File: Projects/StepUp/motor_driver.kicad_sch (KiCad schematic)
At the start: 39 parts, among them J3 1862068, Q1 BSS84, Q2 2N7002-7-F, U4 TMC2300-LA

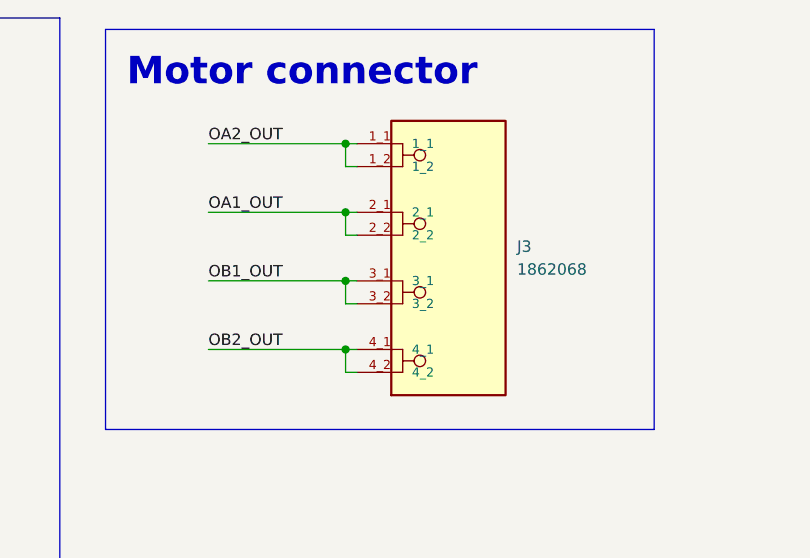
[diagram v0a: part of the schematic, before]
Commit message: feat(cad): CAD dims pushed to PCB
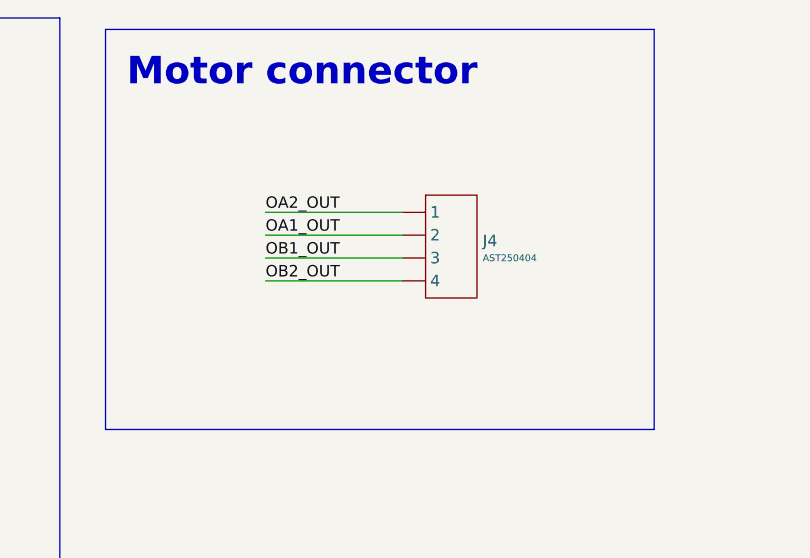
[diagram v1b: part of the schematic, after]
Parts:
- removed J3: 1862068, Snapeda:1862068_PHOENIX_1862068, symbol Snapeda_kicad:1862068
- added J4: AST250404, my_parts:AST250404, symbol my_parts:AST250404
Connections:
- net OA1_OUT: now also J4. (4)
- net OA2_OUT: now also J4. (4)
- net OB1_OUT: now also J4. (4)
- net OB2_OUT: now also J4. (4)

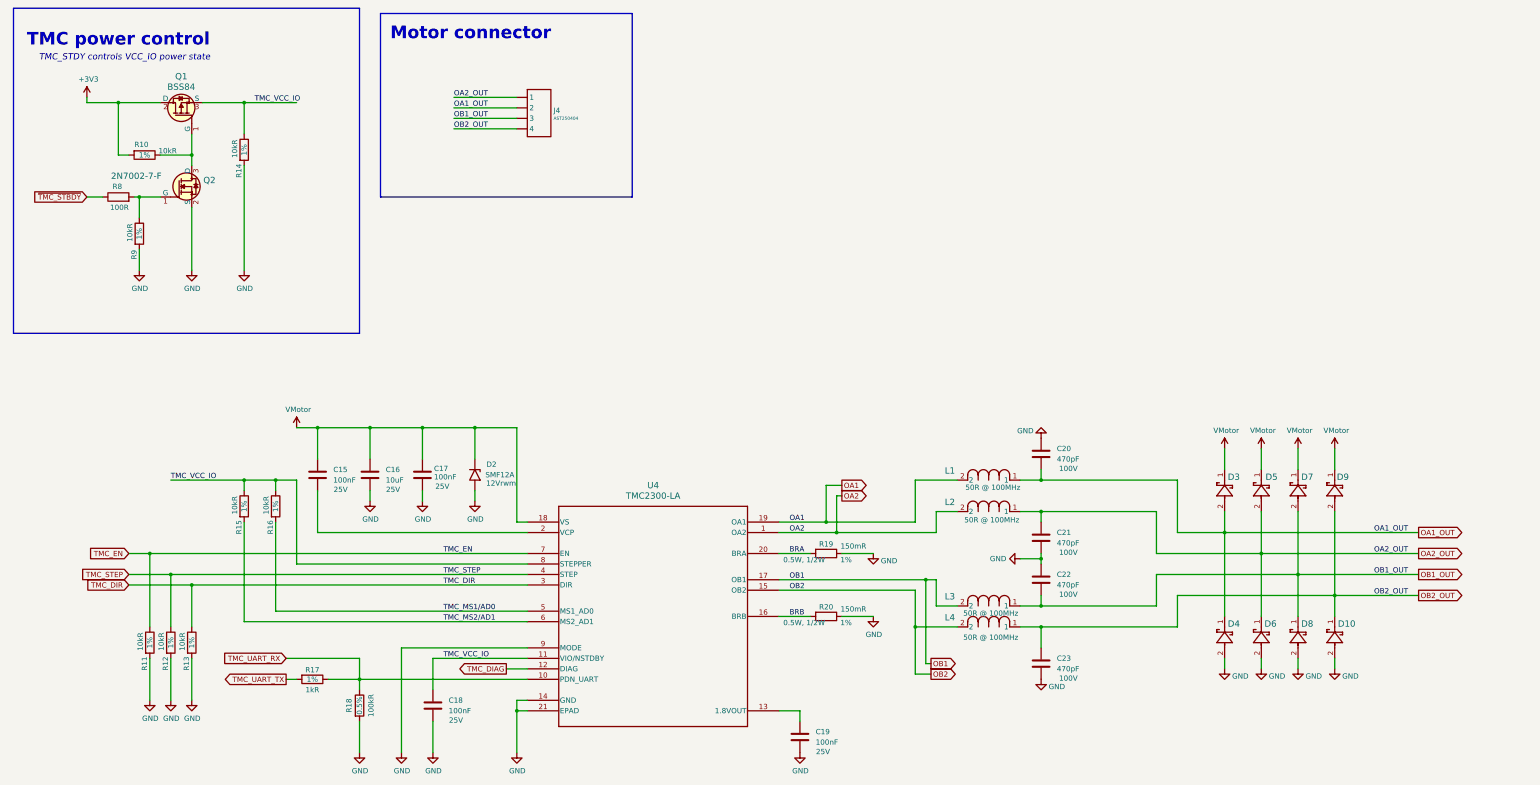
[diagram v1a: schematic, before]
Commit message: feat(v0.2): Component layout from CAD
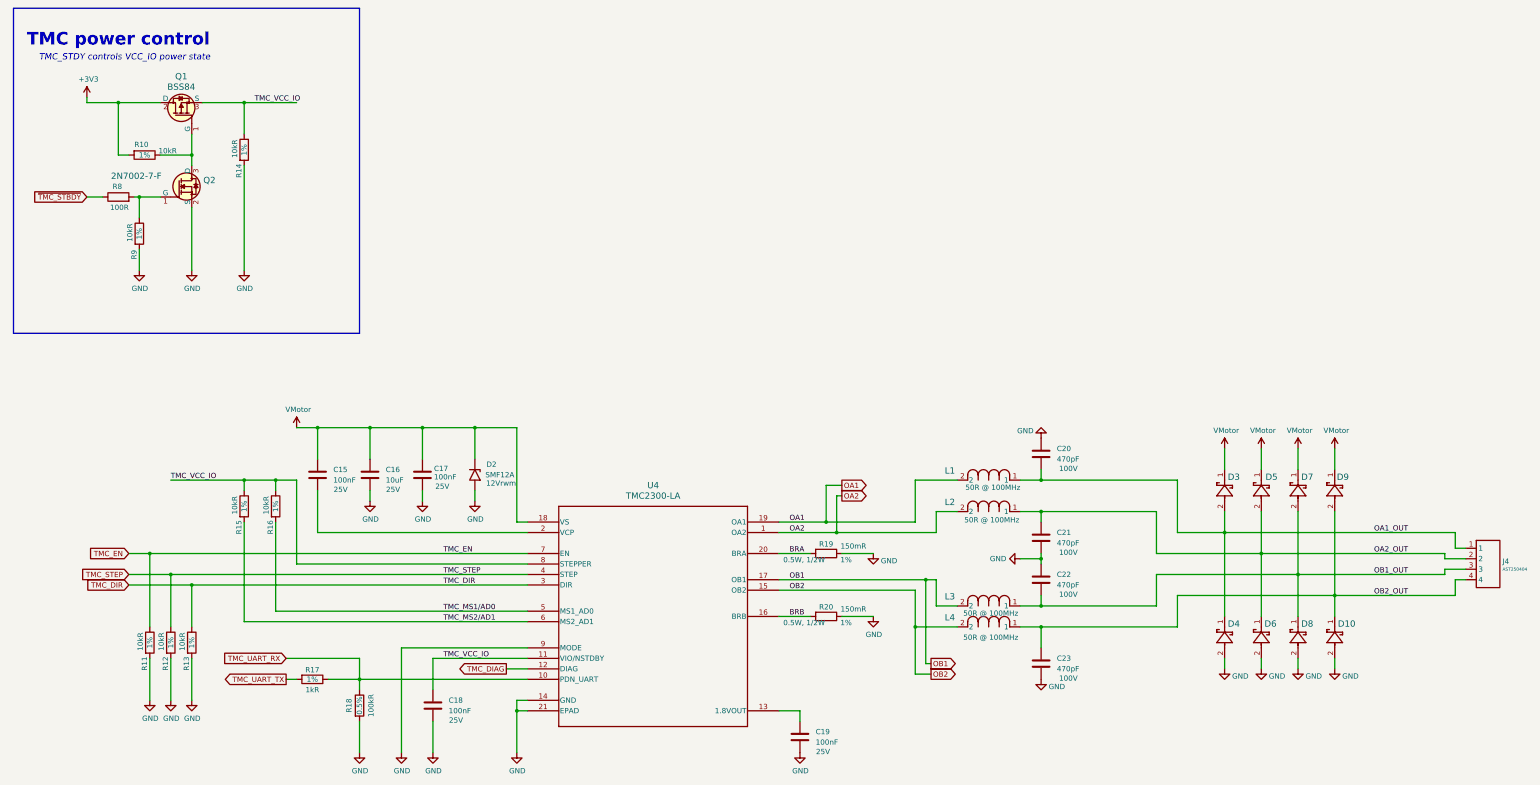
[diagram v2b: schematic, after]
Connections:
- net OA1_OUT: now also J4.1; no longer J4. (4)
- net OA2_OUT: now also J4.2; no longer J4. (4)
- net OB1_OUT: now also J4.3; no longer J4. (4)
- net OB2_OUT: now also J4.4; no longer J4. (4)
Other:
- note removed: "Motor connector"
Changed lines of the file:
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@@
 	(wire
 		(pts
-			(xy 340.36 165.1) (xy 360.68 165.1)
+			(xy 340.36 165.1) (xy 369.57 165.1)
 		)
 		(stroke
@@
 	(wire
 		(pts
+			(xy 369.57 165.1) (xy 369.57 161.29)
+		)
+		(stroke
+			(width 0)
+			(type default)
+		)
+	)
+	(wire
+		(pts
 			(xy 220.98 170.18) (xy 228.6 170.18)
 		)
@@
 	(wire
 		(pts
-			(xy 331.47 160.02) (xy 360.68 160.02)
+			(xy 331.47 160.02) (xy 367.03 160.02)
 		)
 		(stroke
@@
 	(wire
 		(pts
-			(xy 322.58 154.94) (xy 360.68 154.94)
+			(xy 322.58 154.94) (xy 367.03 154.94)
 		)
 		(stroke
@@
 	(wire
 		(pts
+			(xy 367.03 158.75) (xy 372.11 158.75)
+		)
+		(stroke
+			(width 0)
+			(type default)
+		)
+	)
+	(wire
+		(pts
 			(xy 219.71 140.97) (xy 219.71 149.86)
 		)
@@
 	(wire
 		(pts
-			(xy 313.69 149.86) (xy 360.68 149.86)
+			(xy 313.69 149.86) (xy 369.57 149.86)
 		)
 		(stroke
@@
 	(wire
 		(pts
-			(xy 243.84 161.29) (xy 241.3 161.29)
+			(xy 369.57 149.86) (xy 369.57 153.67)
 		)
 		(stroke
@@
 	(wire
 		(pts
-			(xy 132.08 124.46) (xy 132.08 132.08)
+			(xy 243.84 161.29) (xy 241.3 161.29)
 		)
 		(stroke
@@
 	(wire
 		(pts
-			(xy 106.68 139.7) (xy 106.68 142.24)
+			(xy 132.08 124.46) (xy 132.08 132.08)
 		)
 		(stroke
@@
 	(wire
 		(pts
-			(xy 104.14 195.58) (xy 104.14 203.2)
+			(xy 106.68 139.7) (xy 106.68 142.24)
 		)
 		(stroke
@@
 	(wire
 		(pts
-			(xy 242.57 181.61) (xy 241.3 181.61)
+			(xy 104.14 195.58) (xy 104.14 203.2)
 		)
 		(stroke
@@
 	(wire
 		(pts
-			(xy 127 44.45) (xy 142.24 44.45)
+			(xy 242.57 181.61) (xy 241.3 181.61)
 		)
 		(stroke
@@
 	(wire
 		(pts
-			(xy 127 49.53) (xy 142.24 49.53)
-		)
-		(stroke
-			(width 0)
-			(type default)
-		)
-	)
-	(wire
-		(pts
 			(xy 121.92 187.96) (xy 121.92 180.34)
 		)
@@
 	(wire
 		(pts
+			(xy 369.57 153.67) (xy 372.11 153.67)
+		)
+		(stroke
+			(width 0)
+			(type default)
+		)
+	)
+	(wire
+		(pts
 			(xy 63.5 58.42) (xy 63.5 60.96)
 		)
@@
 	(wire
 		(pts
-			(xy 269.24 172.72) (xy 269.24 177.8)
+			(xy 369.57 161.29) (xy 372.11 161.29)
 		)
 		(stroke
@@
 	(wire
 		(pts
-			(xy 58.42 137.16) (xy 76.2 137.16)
+			(xy 269.24 172.72) (xy 269.24 177.8)
 		)
 		(stroke
@@
 	(wire
 		(pts
-			(xy 269.24 167.64) (xy 297.18 167.64)
+			(xy 58.42 137.16) (xy 76.2 137.16)
 		)
 		(stroke
@@
 	(wire
 		(pts
-			(xy 127 52.07) (xy 142.24 52.07)
+			(xy 269.24 167.64) (xy 297.18 167.64)
 		)
 		(stroke
@@
 	(wire
 		(pts
+			(xy 367.03 156.21) (xy 372.11 156.21)
+		)
+		(stroke
+			(width 0)
+			(type default)
+		)
+	)
+	(wire
+		(pts
 			(xy 76.2 137.16) (xy 76.2 139.7)
 		)
@@
 	(wire
 		(pts
-			(xy 127 46.99) (xy 142.24 46.99)
+			(xy 243.84 144.78) (xy 243.84 149.86)
 		)
 		(stroke
@@
 	(wire
 		(pts
-			(xy 243.84 144.78) (xy 243.84 149.86)
+			(xy 367.03 160.02) (xy 367.03 158.75)
 		)
 		(stroke
@@
 	(wire
 		(pts
+			(xy 367.03 154.94) (xy 367.03 156.21)
+		)
+		(stroke
+			(width 0)
+			(type default)
+		)
+	)
+	(wire
+		(pts
 			(xy 144.78 147.32) (xy 142.24 147.32)
 		)
@@
 		)
 	)
-	(rectangle
-		(start 109.22 24.13)
-		(end 170.18 68.58)
-		(stroke
-			(width 0)
-			(type default)
-		)
-		(fill
-			(type none)
-		)
-	)
-	(text "Motor connector"
-		(exclude_from_sim no)
-		(at 131.064 28.956 0)
-		(effects
-			(font
-				(face "KiCad Font")
-				(size 3.048 3.048)
-				(thickness 0.254)
-				(bold yes)
-				(color 29 232 255 1)
-			)
-		)
-	)
 	(text "TMC_STDY controls VCC_IO power state"
 		(exclude_from_sim no)
@@
 	)
 	(label "OA2_OUT"
-		(at 127 44.45 0)
-		(fields_autoplaced yes)
-		(effects
-			(font
-				(size 1.27 1.27)
-			)
-			(justify left bottom)
-		)
-	)
-	(label "OA2_OUT"
 		(at 358.14 154.94 180)
 		(fields_autoplaced yes)
@@
 		)
 	)
-	(label "OB1_OUT"
-		(at 127 49.53 0)
-		(fields_autoplaced yes)
-		(effects
-			(font
-				(size 1.27 1.27)
-			)
-			(justify left bottom)
-		)
-	)
 	(label "TMC_VCC_IO"
 		(at 78.74 45.72 0)
@@
 		)
 	)
-	(label "OB2_OUT"
-		(at 127 52.07 0)
-		(fields_autoplaced yes)
-		(effects
-			(font
-				(size 1.27 1.27)
-			)
-			(justify left bottom)
-		)
-	)
-	(label "OA1_OUT"
-		(at 127 46.99 0)
-		(fields_autoplaced yes)
-		(effects
-			(font
-				(size 1.27 1.27)
-			)
-			(justify left bottom)
-		)
-	)
 	(label "TMC_MS1{slash}AD0"
 		(at 124.46 168.91 0)
@@
 		)
 	)
-	(global_label "OA2_OUT"
-		(shape output)
-		(at 360.68 154.94 0)
-		(fields_autoplaced yes)
-		(effects
-			(font
-				(size 1.27 1.27)
-				(color 132 0 0 1)
-			)
-			(justify left)
-		)
-		(property "Intersheetrefs" "${INTERSHEET_REFS}"
-			(at 371.89 154.94 0)
-			(effects
-				(font
-					(size 1.27 1.27)
-				)
-				(justify left)
-				(hide yes)
-			)
-		)
-	)
 	(global_label "TMC_DIAG"
 		(shape output)
@@
 		)
 	)
-	(global_label "OB2_OUT"
-		(shape output)
-		(at 360.68 165.1 0)
-		(fields_autoplaced yes)
-		(effects
-			(font
-				(size 1.27 1.27)
-				(color 132 0 0 1)
-			)
-			(justify left)
-		)
-		(property "Intersheetrefs" "${INTERSHEET_REFS}"
-			(at 372.0714 165.1 0)
-			(effects
-				(font
-					(size 1.27 1.27)
-				)
-				(justify left)
-				(hide yes)
-			)
-		)
-	)
 	(global_label "OB2"
 		(shape output)
@@
 		)
 	)
-	(global_label "OA1_OUT"
-		(shape output)
-		(at 360.68 149.86 0)
-		(fields_autoplaced yes)
-		(effects
-			(font
-				(size 1.27 1.27)
-				(color 132 0 0 1)
-			)
-			(justify left)
-		)
-		(property "Intersheetrefs" "${INTERSHEET_REFS}"
-			(at 371.89 149.86 0)
-			(effects
-				(font
-					(size 1.27 1.27)
-				)
-				(justify left)
-				(hide yes)
-			)
-		)
-	)
 	(global_label "TMC_UART_TX"
 		(shape output)
@@
 		)
 	)
-	(global_label "OB1_OUT"
-		(shape output)
-		(at 360.68 160.02 0)
-		(fields_autoplaced yes)
-		(effects
-			(font
-				(size 1.27 1.27)
-				(color 132 0 0 1)
-			)
-			(justify left)
-		)
-		(property "Intersheetrefs" "${INTERSHEET_REFS}"
-			(at 372.0714 160.02 0)
-			(effects
-				(font
-					(size 1.27 1.27)
-				)
-				(justify left)
-				(hide yes)
-			)
-		)
-	)
 	(global_label "TMC_STEP"
 		(shape input)
@@
 	(symbol
 		(lib_id "my_parts:AST250404")
-		(at 142.24 44.45 0)
+		(at 372.11 153.67 0)
 		(unit 1)
 		(exclude_from_sim no)
@@
 		(fields_autoplaced yes)
 		(property "Reference" "J4"
-			(at 151.13 47.6249 0)
+			(at 381 156.8449 0)
 			(effects
 				(font
@@
 		)
 		(property "Value" "AST250404"
-			(at 151.13 49.53 0)
+			(at 381 158.75 0)
 			(effects
 				(font
@@
 		)
 		(property "Footprint" "my_parts:AST250404"
-			(at 170.434 68.326 0)
+			(at 400.304 177.546 0)
 			(effects
 				(font
@@
 		)
 		(property "Datasheet" "https://media.metz-connect.com/index.php?itno=AST025&type=datasheet&language=en"
-			(at 147.574 59.436 0)
+			(at 377.444 168.656 0)
 			(effects
 				(font
@@
 		)
 		(property "Description" "Wire-To-Board Terminal Block, 5 mm, 4 Ways, 28 AWG, 14 AWG, 1 mm², Push In Lock"
-			(at 146.05 64.262 0)
+			(at 375.92 173.482 0)
 			(effects
 				(font
@@
 		)
 		(property "Manufacturer" "METZ-CONNECTOR"
-			(at 135.636 68.326 0)
+			(at 365.506 177.546 0)
 			(effects
 				(font
@@
 		)
 		(property "MPN" "AST250404"
-			(at 151.892 68.326 0)
+			(at 381.762 177.546 0)
 			(effects
 				(font
@@
 			)
 		)
-		(pin ""
+		(pin "3"
 		)
-		(pin ""
+		(pin "4"
 		)
-		(pin ""
+		(pin "1"
 		)
-		(pin ""
+		(pin "2"
 		)
 		(instances

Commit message: feat(layout): Layout begins
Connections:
- net OA1_OUT: now also J4.2; no longer J4.1
- net OA2_OUT: now also J4.1; no longer J4.2
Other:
- note added: "Motor connector"

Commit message: feat(v0.2): Release, PCBs ordered!
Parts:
- J4: value AST250404 -> AST0250404; MPN AST250404 -> AST0250404
- U4: value TMC2300-LA -> TMC2300-LA-T; MPN TMC2300-LA -> TMC2300-LA-T; Manufacturer Analog Devices Inc./Maxim Integrated -> ADI Trinamic

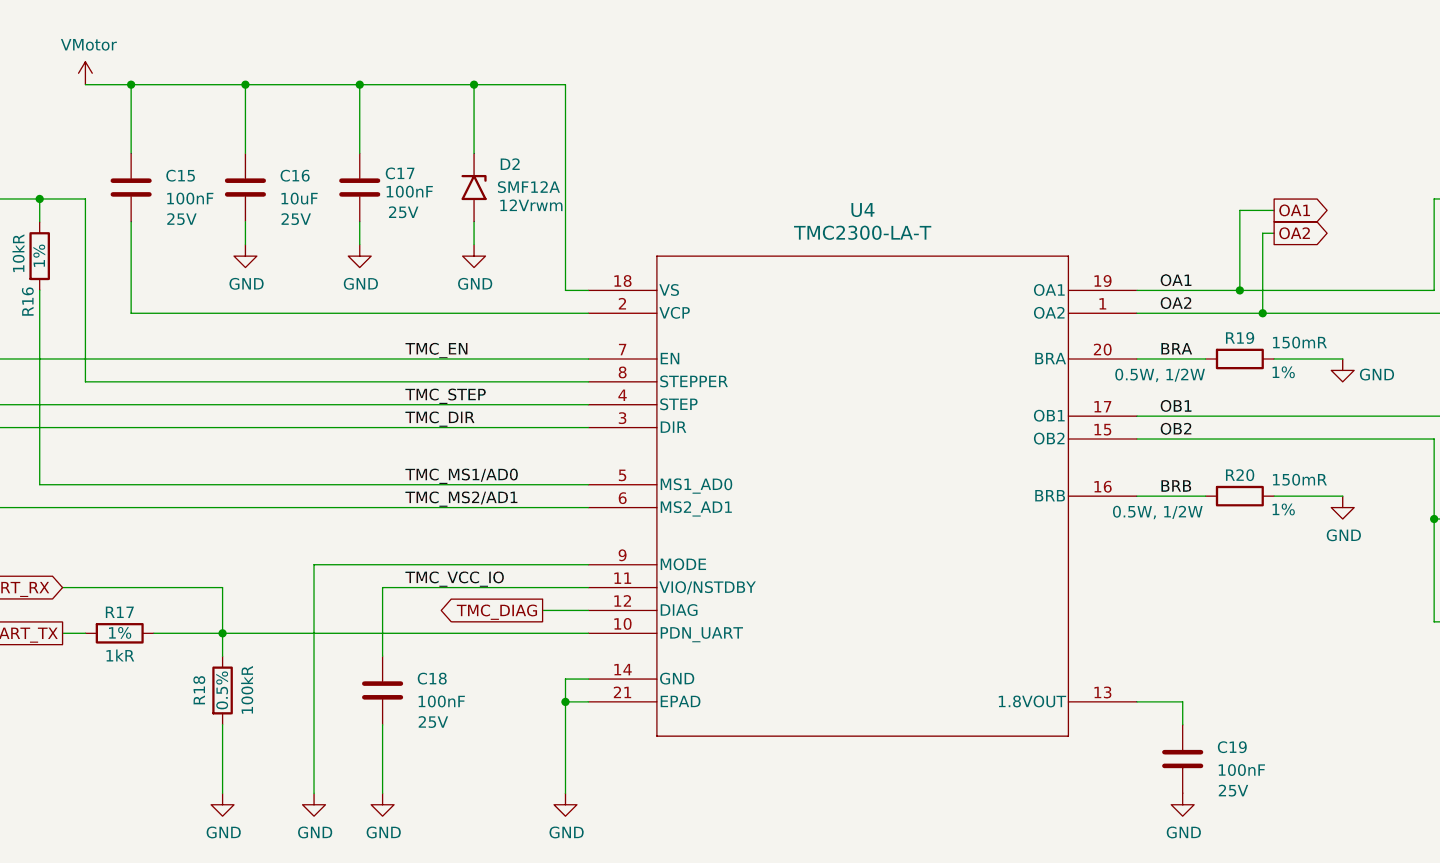
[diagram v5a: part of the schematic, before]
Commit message: feat(v0.3): Boost layout complete
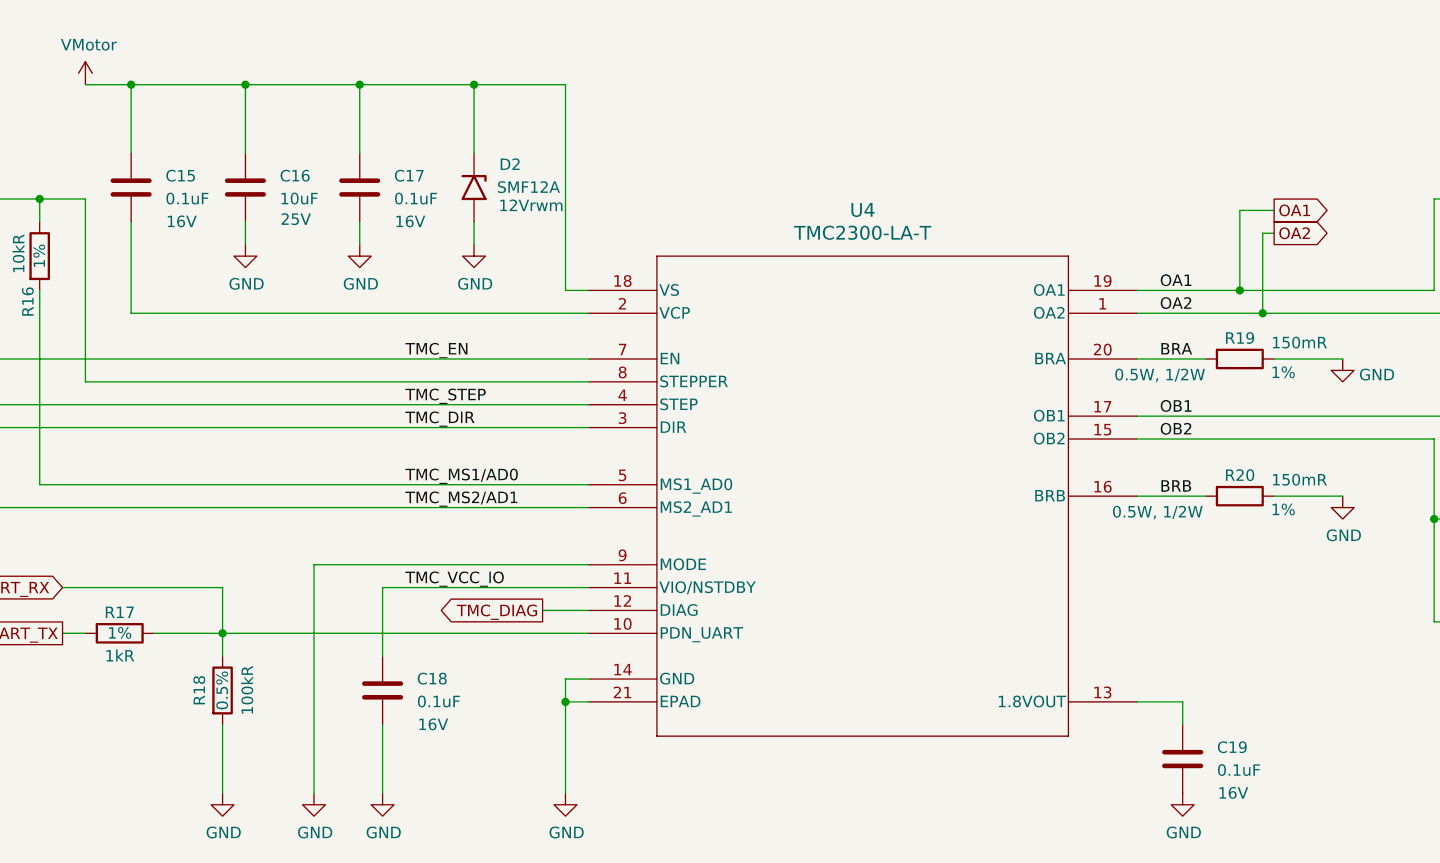
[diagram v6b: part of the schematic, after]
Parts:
- C15, C17, C18, C19: value 100nF -> 0.1uF; Dielectric X7R -> X5R; MPN CC0402KRX7R8BB104 -> GRM155R61C104KA88D; Manufacturer YAGEO -> Murata; Package 0402 -> 0402; Voltage 25V -> 16V

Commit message: feat(v0.3): Layout 90% complete
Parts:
- renumbered J4 to J5
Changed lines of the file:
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@@
 		(on_board yes)
 		(dnp no)
-		(property "Reference" "J4"
+		(property "Reference" "J5"
 			(at 142.748 40.132 0)
 			(effects
@@
 			(project "StepUp"
 				(path "/e0cca1c7-c263-49eb-8c40-74000ebe5285/f5cf6bff-0c76-4311-a1f3-856e1fd3b2e7"
-					(reference "J4")
+					(reference "J5")
 					(unit 1)
 				)

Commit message: feat(v0.3): Files sent to PCBWay for build
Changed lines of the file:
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@@
-		)
-	)
-	(label "TMC_VCC_IO"
-		(at 78.74 45.72 0)
-		(effects
-			(font
-				(size 1.27 1.27)
-			)
-			(justify left bottom)
 		)
 	)
@@
 		)
 	)
+	(label "TMC_VCC_IO"
+		(at 88.9 45.72 180)
+		(effects
+			(font
+				(size 1.27 1.27)
+			)
+			(justify right bottom)
+		)
+	)
